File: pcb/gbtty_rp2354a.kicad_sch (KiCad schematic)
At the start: 37 parts, among them J1 USB_C_Receptacle_USB2.0_16P, J2 SM03B-SRSS-TB, J3 GameBoy_LinkPort, SW1 SW_Push, U2 NCP1117-3.3_SOT223, U3 RP2354A, U4 ADG3304, Y1 ABM8-272-T3

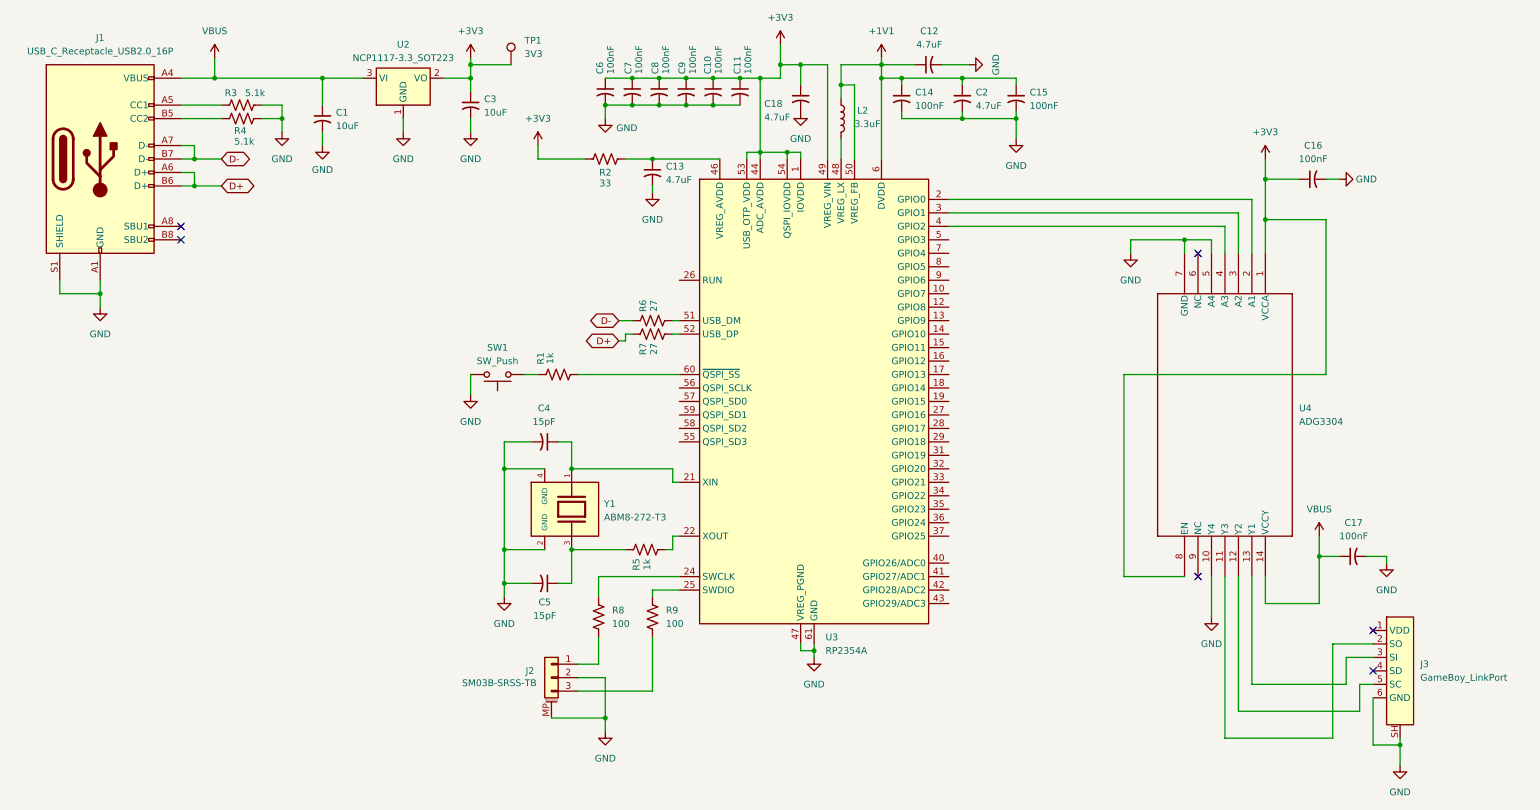
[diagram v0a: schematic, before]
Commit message: pcb: Put the rp2354a design in the shrink-ray
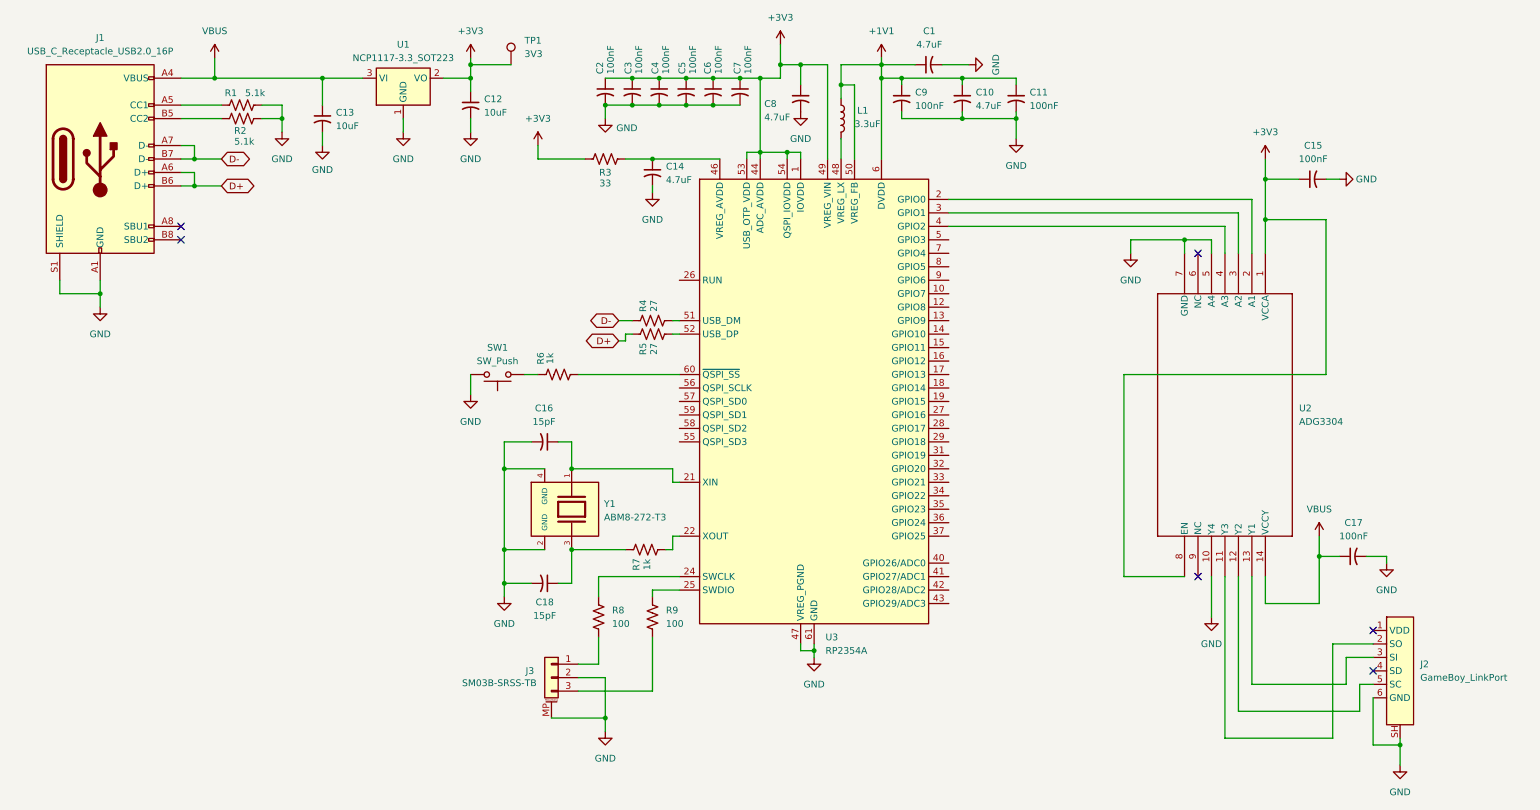
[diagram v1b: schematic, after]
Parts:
- renumbered C12 to C1, C2 to C10, C15 to C11, C3 to C12, C1 to C13, C13 to C14, C16 to C15, C4 to C16, C5 to C18, C6 to C2, C7 to C3, C8 to C4, C9 to C5, C10 to C6, C11 to C7, C18 to C8, C14 to C9, J3 to J2, J2 to J3, L2 to L1, R3 to R1, R4 to R2, R2 to R3, R6 to R4, R7 to R5, R1 to R6, R5 to R7, U2 to U1, U4 to U2
